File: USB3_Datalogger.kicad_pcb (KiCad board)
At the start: 6 copper layers, 57.3 x 37 mm, 57 parts, among them J101 Conn_02x07_Odd_Even, J102 Conn_02x07_Odd_Even, J103 Conn_02x07_Odd_Even, J104 Conn_02x07_Odd_Even, J201 USB3-micro, J301 Conn_01x07, U201 FT600, U202 TPD2EUSB30, U203 TPD2EUSB30, U204 TPD2EUSB30, U301 ICE40HX1K-TQ144, U302 W25Q32JVZP, Y201 30MHz

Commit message: PCB complete, ready for review.
Signed-off-by: Alexis Jeandet <alexis.jeandet@member.fsf.org>
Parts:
- removed J103, J104: Conn_02x07_Odd_Even, Connector_PinHeader_2.54mm:PinHeader_2x07_P2.54mm_Vertical
- added C101: C, Capacitor_SMD:C_0603_1608Metric_Pad1.05x0.95mm_HandSolder, B.Cu at (103.6, 188.4)
- added C102: C, Capacitor_SMD:C_0603_1608Metric_Pad1.05x0.95mm_HandSolder, B.Cu at (107.4, 188.4)
- added C316: 100nF, Capacitor_SMD:C_0402_1005Metric, B.Cu at (131.1, 178.2)
- added C401: 10uF, Capacitor_SMD:C_1206_3216Metric_Pad1.42x1.75mm_HandSolder, F.Cu at (97.7, 154.9)
- added C402: 10uF, Capacitor_SMD:C_1206_3216Metric_Pad1.42x1.75mm_HandSolder, B.Cu at (93.6, 156.8)
- added C403: 10uF, Capacitor_SMD:C_1206_3216Metric_Pad1.42x1.75mm_HandSolder, B.Cu at (93.6, 150.0)
- added C404: 10uF, Capacitor_SMD:C_1206_3216Metric_Pad1.42x1.75mm_HandSolder, B.Cu at (107.8, 155.2)
- added C405: 10uF, Capacitor_SMD:C_1206_3216Metric_Pad1.42x1.75mm_HandSolder, B.Cu at (114.2, 155.1)
- added D101: LED, Resistor_SMD:R_0603_1608Metric_Pad1.05x0.95mm_HandSolder, F.Cu at (116.0, 189.9)
- added D102: LED, Resistor_SMD:R_0603_1608Metric_Pad1.05x0.95mm_HandSolder, F.Cu at (114.2, 189.9)
- added L401: 2.2uH, Inductor_SMD:L_1206_3216Metric_Pad1.42x1.75mm_HandSolder, F.Cu at (93.6, 150.0)
- added L402: 2.2uH, Inductor_SMD:L_1206_3216Metric_Pad1.42x1.75mm_HandSolder, F.Cu at (93.6, 156.8)
- added R101: 2K2, Resistor_SMD:R_0402_1005Metric, F.Cu at (116.0, 192.6)
- added R102: 2K2, Resistor_SMD:R_0402_1005Metric, F.Cu at (114.2, 192.6)
- added R103: 2K2, Resistor_SMD:R_0402_1005Metric, F.Cu at (103.6, 185.4)
- added R104: 2K2, Resistor_SMD:R_0402_1005Metric, F.Cu at (107.4, 185.4)
- added REF**: KiCad-Logo2_6mm_SilkScreen, Symbol:KiCad-Logo2_6mm_SilkScreen, F.Cu at (91.2, 189.1)
- added REF**: OSHW-Logo2_9.8x8mm_SilkScreen, Symbol:OSHW-Logo2_9.8x8mm_SilkScreen, F.Cu at (87.5, 181.7)
- added SW101: SW_Push, Button_Switch_SMD:SW_SPST_B3U-1000P, F.Cu at (103.6, 189.2)
- added SW102: SW_Push, Button_Switch_SMD:SW_SPST_B3U-1000P, F.Cu at (107.4, 189.2)
- added U401: tps6240x, Package_SON:Texas_S-PVSON-N10_ThermalVias, F.Cu at (93.6, 153.4)
- added U402: TLV73325PDBV, Package_TO_SOT_SMD:SOT-23-5, B.Cu at (111.0, 155.7)
- C201, C202, C203, C204, C205, C207, C210, C211, C212, C213, C214, C215, C216, C217, C301, C302, C303, C304, C306, C307, C308, C309, C310, C311, C312, C313, C314, C315, R201, R202, R203, R301, R302, R303, R304, R305, U302, Y201: moved to B.Cu
- C206, C208, C209, C305, J201, U201, U202, U203, U301: moved to F.Cu
- J101: value Conn_02x07_Odd_Even -> Conn_02x20_Odd_Even; footprint Connector_PinHeader_2.54mm:PinHeader_2x07_P2.54mm_Vertical -> Connector_PinHeader_2.54mm:PinHeader_2x20_P2.54mm_Vertical
- U204: value TPD2EUSB30 -> USB6B1; footprint Package_TO_SOT_SMD:Texas_DRT-3 -> Package_SO:SOIC-8_3.9x4.9mm_P1.27mm; moved to F.Cu
- moved J102 164.8 mm to (124.5, 192.1), turned to 90 degrees
- moved J101 127.2 mm to (145.9, 143.8)
- moved C306 73.2 mm to (134.1, 178.2), turned to 90 degrees
- moved C313 73.2 mm to (129.6, 178.2), turned to 90 degrees
- moved C303 73.0 mm to (119.0, 178.1), turned to 90 degrees
- moved C212 71.2 mm to (100.2, 177.2), turned to 270 degrees
- moved C210 68.2 mm to (105.2, 175.7), turned to 270 degrees
- moved C214 68.2 mm to (101.9, 175.7), turned to 270 degrees
- moved C216 68.2 mm to (104.0, 175.7), turned to 270 degrees
- moved C201 64.3 mm to (100.7, 173.8)
- moved C312 63.7 mm to (134.3, 173.4)
- moved U202 62.5 mm to (89.4, 172.8), turned to 90 degrees
- moved C309 61.7 mm to (116.5, 172.4)
- moved C203 61.2 mm to (109.0, 172.2)
- moved C206 59.7 mm to (88.8, 171.4)
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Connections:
- net Net-(U301-Pad1) renamed /IOL_0
- net Net-(U301-Pad2) renamed /IOL_1
- net Net-(U301-Pad3) renamed /IOL_2
- net Net-(U301-Pad4) renamed /IOL_3
- net Net-(U301-Pad73) renamed /IOR_0
- net Net-(U301-Pad74) renamed /IOR_1
- net Net-(U301-Pad75) renamed /IOR_2
- net Net-(U301-Pad76) renamed /IOR_3
- net Net-(U301-Pad78) renamed /IOR_4
- net Net-(U301-Pad79) renamed /IOR_5
- net Net-(U301-Pad80) renamed /IOR_6
- net Net-(U301-Pad81) renamed /IOR_7
- net Net-(U301-Pad87) renamed /IOR_8
- net Net-(U301-Pad88) renamed /IOR_9
- net Net-(U301-Pad90) renamed /IOR_10
- net Net-(U301-Pad91) renamed /IOR_11
- net Net-(U301-Pad93) renamed /IOR_12
- net Net-(U301-Pad94) renamed /IOR_13
- C209 pad 1: /Sheet5E41F9C9/VBUS -> /VBUS
- C301 pad 1: /Sheet5E4285EB/3.3V -> /3.3V
- C302 pad 1: /Sheet5E4285EB/3.3V -> /3.3V
- C303 pad 1: /Sheet5E4285EB/3.3V -> /3.3V
- C304 pad 1: /Sheet5E4285EB/3.3V -> /3.3V
- C308 pad 1: /Sheet5E4285EB/3.3V -> /3.3V
- C309 pad 1: /Sheet5E4285EB/3.3V -> /3.3V
- C310 pad 1: /Sheet5E4285EB/3.3V -> /3.3V
- C311 pad 1: /Sheet5E4285EB/3.3V -> /3.3V
- C312 pad 1: /Sheet5E4285EB/3.3V -> /3.3V
- J101 pad 1: Net-(J101-Pad1) -> GND
- J101 pad 10: Net-(J101-Pad10) -> /IOR_19
- J101 pad 11: Net-(J101-Pad11) -> /IOR_16
- J101 pad 12: Net-(J101-Pad12) -> /IOR_17
- J101 pad 13: Net-(J101-Pad13) -> /IOR_14
- J101 pad 14: Net-(J101-Pad14) -> /IOR_15
- J101 pad 2: Net-(J101-Pad2) -> GND
- J101 pad 3: Net-(J101-Pad3) -> /VBUS
- J101 pad 4: Net-(J101-Pad4) -> /VBUS
- J101 pad 5: Net-(J101-Pad5) -> /3.3V
- J101 pad 6: Net-(J101-Pad6) -> /3.3V
- J101 pad 7: Net-(J101-Pad7) -> /IOR_20
- J101 pad 8: Net-(J101-Pad8) -> /IOR_21
- J101 pad 9: Net-(J101-Pad9) -> /IOR_18
- J102 pad 1: Net-(J102-Pad1) -> /IOL_8
- J102 pad 10: Net-(J102-Pad10) -> /IOL_17
- J102 pad 11: Net-(J102-Pad11) -> /IOL_18
- J102 pad 12: Net-(J102-Pad12) -> /IOL_19
- J102 pad 13: Net-(J102-Pad13) -> GND
- J102 pad 14: Net-(J102-Pad14) -> GND
- J102 pad 2: Net-(J102-Pad2) -> /IOL_9
- J102 pad 3: Net-(J102-Pad3) -> /IOL_10
- J102 pad 4: Net-(J102-Pad4) -> /IOL_11
- J102 pad 5: Net-(J102-Pad5) -> /IOL_12
- J102 pad 6: Net-(J102-Pad6) -> /IOL_13
- J102 pad 7: Net-(J102-Pad7) -> /IOL_14
- J102 pad 8: Net-(J102-Pad8) -> /IOL_15
- J102 pad 9: Net-(J102-Pad9) -> /IOL_16
- J201 pad 1: /Sheet5E41F9C9/VBUS -> /VBUS
- R301 pad 1: /Sheet5E4285EB/3.3V -> /3.3V
- R302 pad 1: /Sheet5E4285EB/3.3V -> /3.3V
- R303 pad 1: /Sheet5E4285EB/3.3V -> /3.3V
- R304 pad 1: /Sheet5E4285EB/3.3V -> /3.3V
- R305 pad 1: /Sheet5E4285EB/3.3V -> /3.3V
- R306 pad 1: /Sheet5E4285EB/3.3V -> /3.3V
- U201 pad 12: Net-(U201-Pad12) -> /Sheet5E4285EB/FIFO_GPIO_0
- U201 pad 13: Net-(U201-Pad13) -> /Sheet5E4285EB/FIFO_GPIO_1
- U201 pad 29: /Sheet5E41F9C9/VBUS -> /VBUS
- U204 pad 1: /Sheet5E41F9C9/USB2_D+ -> /VBUS
- U204 pad 2: /Sheet5E41F9C9/USB2_D- -> /Sheet5E41F9C9/USB2_D+
- U204 pad 3: GND -> /Sheet5E41F9C9/USB2_D-
- U301 pad 10: Net-(U301-Pad10) -> /IOL_7
- U301 pad 100: /Sheet5E4285EB/3.3V -> /3.3V
- U301 pad 101: Net-(U301-Pad101) -> /IOR_19
- U301 pad 102: Net-(U301-Pad102) -> /IOR_20
- U301 pad 104: Net-(U301-Pad104) -> /IOR_21
- U301 pad 105: Net-(U301-Pad105) -> /Sheet5E4285EB/FIFO_GPIO_1
- U301 pad 106: Net-(U301-Pad106) -> /Sheet5E4285EB/FIFO_GPIO_0
- U301 pad 11: Net-(U301-Pad11) -> /IOL_8
- U301 pad 12: Net-(U301-Pad12) -> /IOL_9
- U301 pad 123: /Sheet5E4285EB/3.3V -> /3.3V
- U301 pad 133: /Sheet5E4285EB/3.3V -> /3.3V
- U301 pad 19: Net-(U301-Pad19) -> /IOL_10
- U301 pad 20: Net-(U301-Pad20) -> /IOL_11
- U301 pad 21: Net-(U301-Pad21) -> /IOL_12
- U301 pad 22: Net-(U301-Pad22) -> /IOL_13
- U301 pad 23: Net-(U301-Pad23) -> /IOL_14
- U301 pad 24: Net-(U301-Pad24) -> /IOL_15
- U301 pad 25: Net-(U301-Pad25) -> /IOL_16
- U301 pad 26: Net-(U301-Pad26) -> /IOL_17
- U301 pad 28: Net-(U301-Pad28) -> /IOL_18
- U301 pad 29: Net-(U301-Pad29) -> /IOL_19
- U301 pad 30: /Sheet5E4285EB/3.3V -> /3.3V
- U301 pad 31: Net-(U301-Pad31) -> /IOL_20
- U301 pad 32: Net-(U301-Pad32) -> /IOL_21
- U301 pad 33: Net-(U301-Pad33) -> /IOL_22
- U301 pad 34: Net-(U301-Pad34) -> /IOL_23
- U301 pad 37: Net-(U301-Pad37) -> /IOB_0
- U301 pad 38: Net-(U301-Pad38) -> /IOB_1
- U301 pad 39: Net-(U301-Pad39) -> /IOB_2
- U301 pad 41: Net-(U301-Pad41) -> /IOB_3
- U301 pad 42: Net-(U301-Pad42) -> /IOB_4
- U301 pad 43: Net-(U301-Pad43) -> /IOB_5
- U301 pad 44: Net-(U301-Pad44) -> /IOB_6
- U301 pad 45: Net-(U301-Pad45) -> /IOB_7
- U301 pad 46: /Sheet5E4285EB/3.3V -> /3.3V
- U301 pad 47: Net-(U301-Pad47) -> /IOB_8
- U301 pad 48: Net-(U301-Pad48) -> /IOB_9
- U301 pad 49: Net-(U301-Pad49) -> /IOB_10
- U301 pad 50: Net-(U301-Pad50) -> /IOB_11
- U301 pad 52: Net-(U301-Pad52) -> /IOB_12
- U301 pad 56: Net-(U301-Pad56) -> /IOB_13
- U301 pad 57: /Sheet5E4285EB/3.3V -> /3.3V
- U301 pad 58: Net-(U301-Pad58) -> /IOB_14
- U301 pad 6: /Sheet5E4285EB/3.3V -> /3.3V
- U301 pad 60: Net-(U301-Pad60) -> /IOB_15
- U301 pad 61: Net-(U301-Pad61) -> /IOB_16
- U301 pad 62: Net-(U301-Pad62) -> /IOB_17
- U301 pad 63: Net-(U301-Pad63) -> /IOB_18
- U301 pad 64: Net-(U301-Pad64) -> /IOB_19
- U301 pad 7: Net-(U301-Pad7) -> /IOL_4
- U301 pad 72: /Sheet5E4285EB/3.3V -> /3.3V
- U301 pad 8: Net-(U301-Pad8) -> /IOL_5
- U301 pad 89: /Sheet5E4285EB/3.3V -> /3.3V
- U301 pad 9: Net-(U301-Pad9) -> /IOL_6
- U301 pad 95: Net-(U301-Pad95) -> /IOR_14
- U301 pad 96: Net-(U301-Pad96) -> /IOR_15
- U301 pad 97: Net-(U301-Pad97) -> /IOR_16
- U301 pad 98: Net-(U301-Pad98) -> /IOR_17
- U301 pad 99: Net-(U301-Pad99) -> /IOR_18
- U302 pad 8: /Sheet5E4285EB/3.3V -> /3.3V
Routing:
- net /VBUS: track 0.00 -> 135.2 mm, vias 0 -> 8
- net /IOR_21: track 0.00 -> 37.1 mm, vias 0 -> 1
- net /IOR_19: track 0.00 -> 34.4 mm, vias 0 -> 1
- net /IOR_20: track 0.00 -> 32.5 mm, vias 0 -> 1
- net /Sheet5E4285EB/1.2V: track 6.01 -> 36.9 mm, vias 5 -> 6
- net /IOR_17: track 0.00 -> 30.2 mm, vias 0 -> 1
- net /IOR_18: track 0.00 -> 29.7 mm, vias 0 -> 1
- net /IOR_15: track 0.00 -> 28.4 mm, vias 0 -> 1
- net /3.3V: track 0.00 -> 28.3 mm, vias 0 -> 21
- net /Sheet5E4285EB/FIFO_GPIO_1: track 0.00 -> 26.4 mm
- net /IOR_16: track 0.00 -> 26.2 mm, vias 0 -> 1
- net /Sheet5E4285EB/FIFO_GPIO_0: track 0.00 -> 24.7 mm
- net /IOR_14: track 0.00 -> 24.6 mm, vias 0 -> 1
- net /IOL_21: track 0.00 -> 21.1 mm
- net /IOL_4: track 0.00 -> 20.8 mm, vias 0 -> 1
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- added copper zone on In1.Cu, net /3.3V
- added copper zone on In3.Cu, net /3.3V
- added copper zone on In2.Cu, net /Sheet5E41F9C9/3.3V
- added copper zone on In3.Cu, net /Sheet5E41F9C9/VD10
- added copper zone on In2.Cu, net /Sheet5E4285EB/1.2V
- added copper zone on F.Cu, net GND
- added copper zone on In1.Cu, net GND
- removed copper zone on In2.Cu, net /Sheet5E41F9C9/VD10
- removed copper zone on In3.Cu, net /Sheet5E4285EB/1.2V
- removed copper zone on In4.Cu, net /Sheet5E4285EB/3.3V
- removed copper zone on In3.Cu, net 3.3V
- removed copper zone on In4.Cu, net GND
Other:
- board size 57.3 x 37 mm -> 68.5 x 53.5 mm
- board text added: "USB3 Datalogger V 1.0 LPP/CNRS"

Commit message: Added Oscillator for the FPGA and updated PCB to match Eurocircuits rules.
Signed-off-by: Alexis Jeandet <alexis.jeandet@member.fsf.org>
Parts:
- added C103: 100nF, Capacitor_SMD:C_0402_1005Metric, F.Cu at (127.8, 153.4)
- added U101: ASDMB-xxxMHz, Oscillator:Oscillator_SMD_Abracon_ASDMB-4Pin_2.5x2.0mm, F.Cu at (125.5, 153.1)
- moved C207 1.07 mm to (99.5, 169.8)
- moved C216 0.74 mm to (103.6, 175.1)
- moved C210 0.72 mm to (105.8, 175.3)
- moved C205 0.55 mm to (100.1, 168.7)
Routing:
- net /3.3V: track 28.3 -> 34.5 mm
- net /IOR_12: track 0.00 -> 4.92 mm
- net /Sheet5E41F9C9/DATA_1: track 14.6 -> 16.4 mm
- net /Sheet5E41F9C9/3.3V: track 17.6 -> 19.3 mm
- net /Sheet5E41F9C9/DATA_0: track 15.3 -> 16.7 mm
- net Net-(C217-Pad1): track 4.23 -> 4.81 mm
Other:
- net class Default: clearance 0.15 -> 0.125
- net class USB3: clearance 0.15 -> 0.125
- rule trace_clearance: 0.15 -> 0.125
- rule via_min_drill: 0.15 -> 0.1

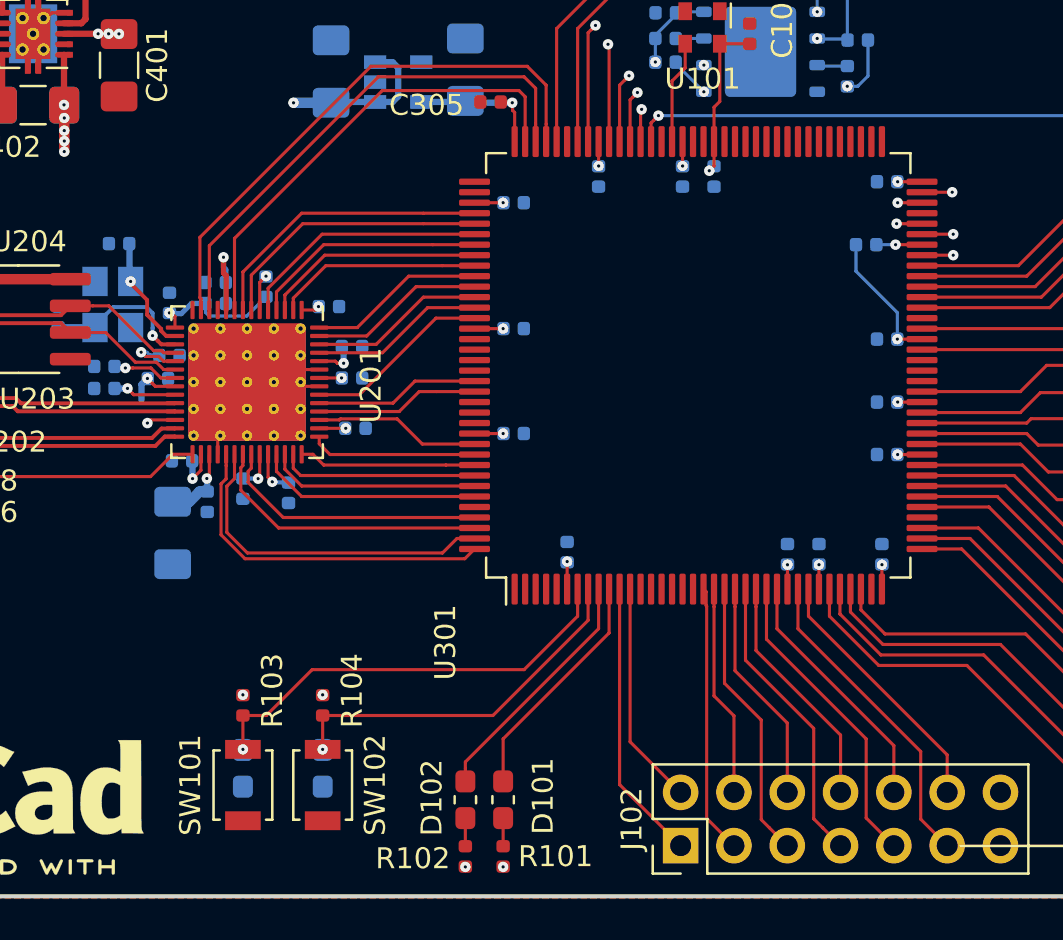
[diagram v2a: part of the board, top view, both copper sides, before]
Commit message: Made the board compatible with HX4K variant
Signed-off-by: Alexis Jeandet <alexis.jeandet@member.fsf.org>
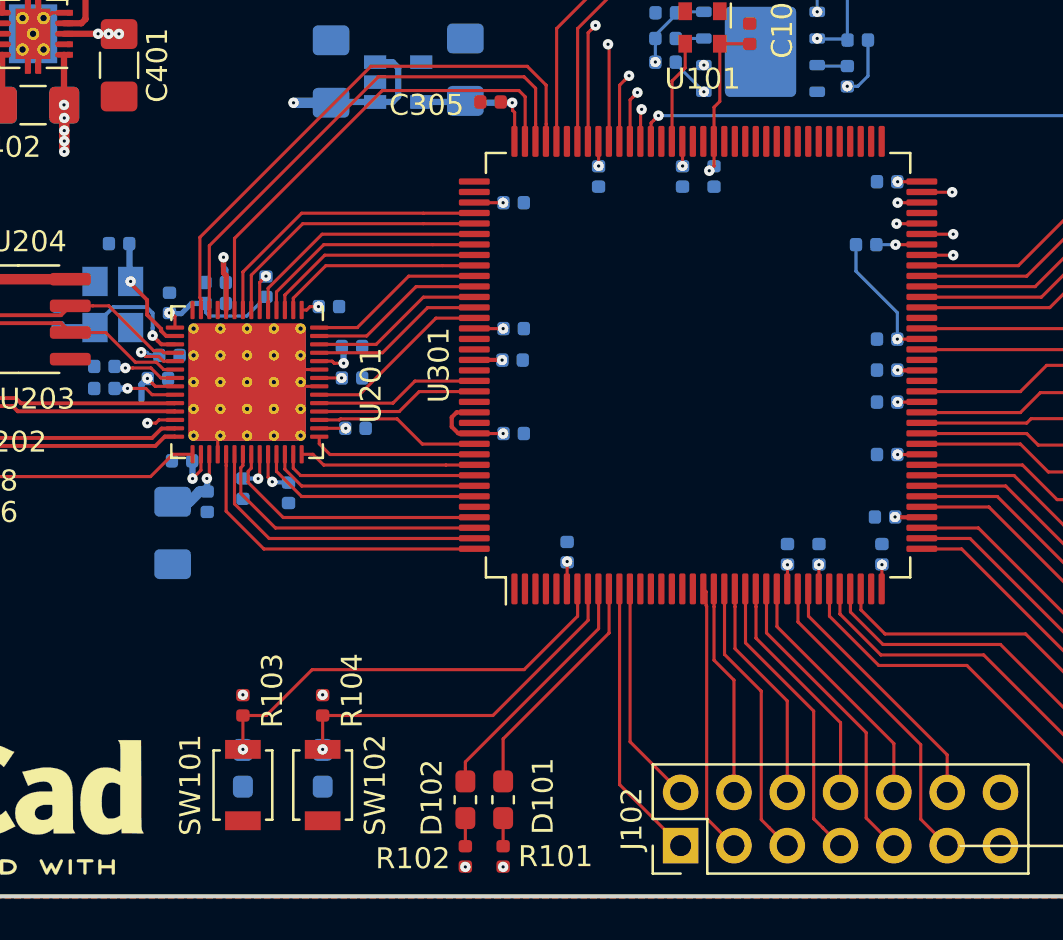
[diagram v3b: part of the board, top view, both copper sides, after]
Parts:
- added C317: 100nF, Capacitor_SMD:C_0402_1005Metric, B.Cu at (134.3, 169.4)
- added C318: 100nF, Capacitor_SMD:C_0402_1005Metric, B.Cu at (134.2, 176.4)
- added C319: 100nF, Capacitor_SMD:C_0402_1005Metric, B.Cu at (116.5, 168.9)
- U301: value ICE40HX1K-TQ144 -> ICE40HX1K-4K-TQ144
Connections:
- C103 pad 1: /3.3V -> VCCIO_0
- C301 pad 1: /3.3V -> VCCIO_0
- C302 pad 1: /3.3V -> VCCIO_0
- C303 pad 1: /3.3V -> VCCIO_0
- C304 pad 1: /3.3V -> VCCIO_0
- C306 pad 1: /Sheet5E4285EB/1.2V -> VCC
- C307 pad 1: /Sheet5E4285EB/1.2V -> VCC
- C308 pad 1: /3.3V -> VCCIO_0
- C309 pad 1: /3.3V -> VCCIO_0
- C310 pad 1: /3.3V -> VCCIO_0
- C311 pad 1: /3.3V -> VCCIO_0
- C312 pad 1: /3.3V -> VCCIO_0
- C313 pad 1: /Sheet5E4285EB/1.2V -> VCC
- C314 pad 1: /Sheet5E4285EB/1.2V -> VCC
- C315 pad 1: /Sheet5E4285EB/1.2V -> VCC
- C316 pad 1: /3.3V -> VCCIO_0
- C402 pad 1: /3.3V -> VCCIO_0
- C403 pad 1: /Sheet5E4285EB/1.2V -> VCC
- J101 pad 5: /3.3V -> VCCIO_0
- J101 pad 6: /3.3V -> VCCIO_0
- L401 pad 2: /Sheet5E4285EB/1.2V -> VCC
- L402 pad 2: /3.3V -> VCCIO_0
- R101 pad 1: /3.3V -> VCCIO_0
- R102 pad 1: /3.3V -> VCCIO_0
- R103 pad 1: /3.3V -> VCCIO_0
- R104 pad 1: /3.3V -> VCCIO_0
- R301 pad 1: /3.3V -> VCCIO_0
- R302 pad 1: /3.3V -> VCCIO_0
- R303 pad 1: /3.3V -> VCCIO_0
- R304 pad 1: /3.3V -> VCCIO_0
- R305 pad 1: /3.3V -> VCCIO_0
- R306 pad 1: /3.3V -> VCCIO_0
- U101 pad 4: /3.3V -> VCCIO_0
- U301 pad 100: /3.3V -> VCCIO_0
- U301 pad 111: /Sheet5E4285EB/1.2V -> VCC
- U301 pad 123: /3.3V -> VCCIO_0
- U301 pad 126: Net-(U301-Pad126) -> VCC
- U301 pad 127: Net-(U301-Pad127) -> GND
- U301 pad 131: Net-(U301-Pad131) -> VCCIO_0
- U301 pad 133: /3.3V -> VCCIO_0
- U301 pad 27: /Sheet5E4285EB/1.2V -> VCC
- U301 pad 30: /3.3V -> VCCIO_0
- U301 pad 36: /Sheet5E4285EB/1.2V -> VCC
- U301 pad 40: Net-(U301-Pad40) -> VCC
- U301 pad 46: /3.3V -> VCCIO_0
- U301 pad 51: /Sheet5E4285EB/1.2V -> VCC
- U301 pad 53: Net-(U301-Pad53) -> GND
- U301 pad 54: Net-(U301-Pad54) -> VCC
- U301 pad 57: /3.3V -> VCCIO_0
- U301 pad 6: /3.3V -> VCCIO_0
- U301 pad 72: /3.3V -> VCCIO_0
- U301 pad 89: /3.3V -> VCCIO_0
- U301 pad 92: /Sheet5E4285EB/1.2V -> VCC
- U302 pad 8: /3.3V -> VCCIO_0
- U401 pad 1: /3.3V -> VCCIO_0
- U401 pad 4: /Sheet5E4285EB/1.2V -> VCC
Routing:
- net VCC: track 0.00 -> 40.6 mm, vias 0 -> 9
- net VCCIO_0: track 0.00 -> 37.3 mm, vias 0 -> 21
- net /Sheet5E4285EB/1.2V: track 36.9 -> 0.00 mm, vias 6 -> 0
- net /3.3V: track 34.5 -> 0.00 mm, vias 21 -> 0
- net /Sheet5E41F9C9/DATA_1: track 16.4 -> 14.5 mm
- net /Sheet5E41F9C9/DATA_0: track 16.7 -> 15.3 mm
- added copper zone on In2.Cu, net GND
- added copper zone on In4.Cu, net GND
- added copper zone on In2.Cu, net VCC
- added copper zone on In1.Cu, net VCCIO_0
- added copper zone on In3.Cu, net VCCIO_0
- removed copper zone on In1.Cu, net /3.3V
- removed copper zone on In3.Cu, net /3.3V
- removed copper zone on In2.Cu, net /Sheet5E4285EB/1.2V
